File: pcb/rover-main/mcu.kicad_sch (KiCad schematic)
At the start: 0 parts

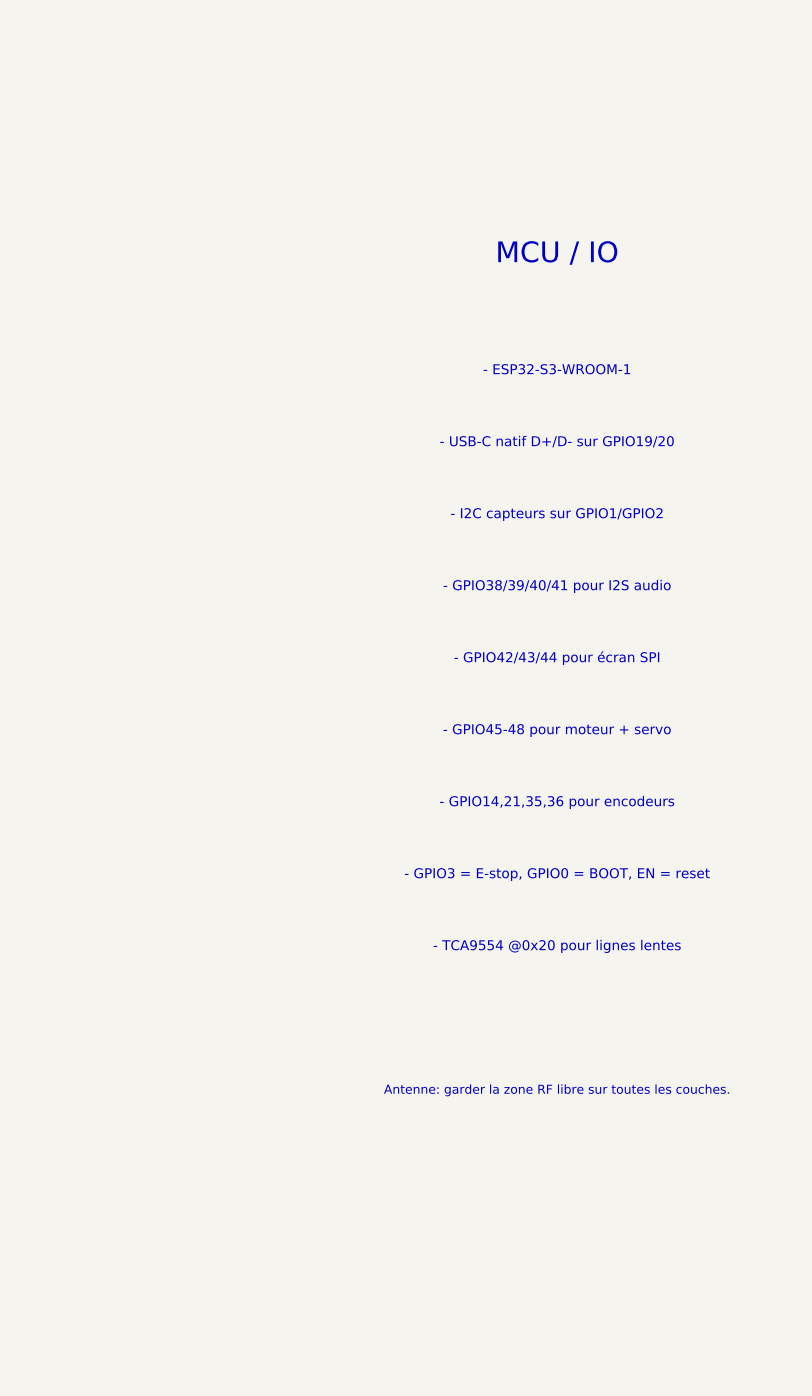
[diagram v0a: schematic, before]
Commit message: Add a more concrete KiCad schematic draft with key blocks and real net names for the Rover PCB design.
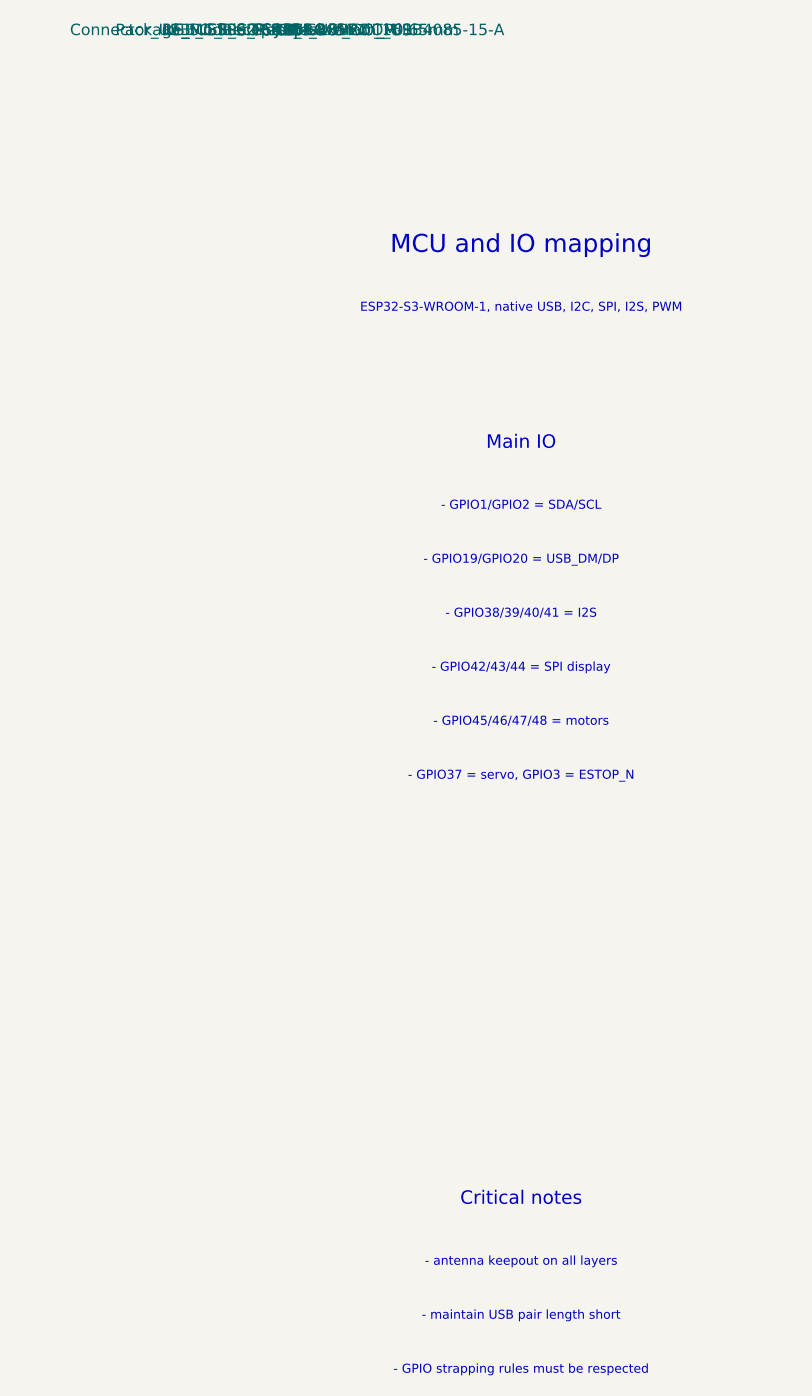
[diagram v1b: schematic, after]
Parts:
- added J10: USB_C_Receptacle_USB2.0_16P, Connector_USB:USB_C_Receptacle_GCT_USB4085-15-A, symbol Connector:USB_C_Receptacle_USB2.0_16P
- added U1: ESP32-S3-WROOM-1, RF_Module:ESP32-S3-WROOM-1, symbol RF_Module:ESP32-S3-WROOM-1
- added U10: TCA9554, Package_SO:TSSOP-16_4.4x5mm_P0.65mm, symbol Interface_Expansion:TCA9554
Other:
- note added: "- GPIO strapping rules must be respected"
- note added: "- GPIO1/GPIO2 = SDA/SCL"
- note added: "- GPIO19/GPIO20 = USB_DM/DP"
- note added: "- GPIO37 = servo, GPIO3 = ESTOP_N"
- note added: "- GPIO38/39/40/41 = I2S"
- note added: "- GPIO42/43/44 = SPI display"
- note added: "- GPIO45/46/47/48 = motors"
- note added: "- antenna keepout on all layers"
- note added: "- maintain USB pair length short"
- note added: "Critical notes"
- note added: "ESP32-S3-WROOM-1, native USB, I2C, SPI, I2S, PWM"
- note added: "MCU and IO mapping"
- note added: "Main IO"
- note removed: "- ESP32-S3-WROOM-1"
- note removed: "- GPIO14,21,35,36 pour encodeurs"
- note removed: "- GPIO3 = E-stop, GPIO0 = BOOT, EN = reset"
- note removed: "- GPIO38/39/40/41 pour I2S audio"
- note removed: "- GPIO42/43/44 pour écran SPI"
- note removed: "- GPIO45-48 pour moteur + servo"
- note removed: "- I2C capteurs sur GPIO1/GPIO2"
- note removed: "- TCA9554 @0x20 pour lignes lentes"
- note removed: "- USB-C natif D+/D- sur GPIO19/20"
- note removed: "Antenne: garder la zone RF libre sur toutes les couches."
- note removed: "MCU / IO"
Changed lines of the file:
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@@
 (kicad_sch
-  (version 20250114)
-  (generator "KiCad")
+  (version 20211014)
+  (generator "eeschema")
   (paper "A4")
   (title_block
     (title "Rover PCB - MCU")
     (date "2026-10-13")
-    (rev "0.1")
+    (rev "0.2")
     (company "Rover Project")
-    (comment 1 "Draft only - validate GPIO mapping")
+    (comment 1 "Draft schematic - validate GPIO mapping with firmware")
   )
-  (text "MCU / IO" (at 30 25 0)
-    (effects (font (size 2.3 2.3) (thickness 0.3)))
+  (text "MCU and IO mapping" (at 26 24 0)
+    (effects (font (size 2.0 2.0) (thickness 0.2)))
   )
-  (text "- ESP32-S3-WROOM-1" (at 30 38 0)
-    (effects (font (size 1.1 1.1)))
-  )
-  (text "- USB-C natif D+/D- sur GPIO19/20" (at 30 46 0)
-    (effects (font (size 1.1 1.1)))
-  )
-  (text "- I2C capteurs sur GPIO1/GPIO2" (at 30 54 0)
-    (effects (font (size 1.1 1.1)))
-  )
-  (text "- GPIO38/39/40/41 pour I2S audio" (at 30 62 0)
-    (effects (font (size 1.1 1.1)))
-  )
-  (text "- GPIO42/43/44 pour écran SPI" (at 30 70 0)
-    (effects (font (size 1.1 1.1)))
-  )
-  (text "- GPIO45-48 pour moteur + servo" (at 30 78 0)
-    (effects (font (size 1.1 1.1)))
-  )
-  (text "- GPIO14,21,35,36 pour encodeurs" (at 30 86 0)
-    (effects (font (size 1.1 1.1)))
-  )
-  (text "- GPIO3 = E-stop, GPIO0 = BOOT, EN = reset" (at 30 94 0)
-    (effects (font (size 1.1 1.1)))
-  )
-  (text "- TCA9554 @0x20 pour lignes lentes" (at 30 102 0)
-    (effects (font (size 1.1 1.1)))
-  )
-  (text "Antenne: garder la zone RF libre sur toutes les couches." (at 30 118 0)
+  (text "ESP32-S3-WROOM-1, native USB, I2C, SPI, I2S, PWM" (at 26 31 0)
     (effects (font (size 1.0 1.0)))
   )
+  (text "Main IO" (at 26 46 0)
+    (effects (font (size 1.5 1.5) (thickness 0.2)))
+  )
+  (text "- GPIO1/GPIO2 = SDA/SCL" (at 26 53 0)
+    (effects (font (size 1.0 1.0)))
+  )
+  (text "- GPIO19/GPIO20 = USB_DM/DP" (at 26 59 0)
+    (effects (font (size 1.0 1.0)))
+  )
+  (text "- GPIO38/39/40/41 = I2S" (at 26 65 0)
+    (effects (font (size 1.0 1.0)))
+  )
+  (text "- GPIO42/43/44 = SPI display" (at 26 71 0)
+    (effects (font (size 1.0 1.0)))
+  )
+  (text "- GPIO45/46/47/48 = motors" (at 26 77 0)
+    (effects (font (size 1.0 1.0)))
+  )
+  (text "- GPIO37 = servo, GPIO3 = ESTOP_N" (at 26 83 0)
+    (effects (font (size 1.0 1.0)))
+  )
+  (symbol
+    (lib_id "RF_Module:ESP32-S3-WROOM-1")
+    (at 140 105 0)
+    (unit 1)
+    (in_bom yes)
+    (property "Reference" "U1")
+    (property "Value" "ESP32-S3-WROOM-1")
+    (property "Footprint" "RF_Module:ESP32-S3-WROOM-1")
+  )
+  (symbol
+    (lib_id "Connector:USB_C_Receptacle_USB2.0_16P")
+    (at 295 105 0)
+    (unit 1)
+    (in_bom yes)
+    (property "Reference" "J10")
+    (property "Value" "USB_C_Receptacle_USB2.0_16P")
+    (property "Footprint" "Connector_USB:USB_C_Receptacle_GCT_USB4085-15-A")
+  )
+  (symbol
+    (lib_id "Interface_Expansion:TCA9554")
+    (at 220 180 0)
+    (unit 1)
+    (in_bom yes)
+    (property "Reference" "U10")
+    (property "Value" "TCA9554")
+    (property "Footprint" "Package_SO:TSSOP-16_4.4x5mm_P0.65mm")
+  )
+  (text "Critical notes" (at 26 130 0)
+    (effects (font (size 1.5 1.5) (thickness 0.2)))
+  )
+  (text "- antenna keepout on all layers" (at 26 137 0)
+    (effects (font (size 1.0 1.0)))
+  )
+  (text "- maintain USB pair length short" (at 26 143 0)
+    (effects (font (size 1.0 1.0)))
+  )
+  (text "- GPIO strapping rules must be respected" (at 26 149 0)
+    (effects (font (size 1.0 1.0)))
+  )
